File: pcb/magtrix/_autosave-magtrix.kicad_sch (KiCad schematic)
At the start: 24 parts, among them J2 Conn_01x03_Pin, J3 Conn_01x03_Pin, Q14 BUK6D120, Q15 BUK6D120-60PX

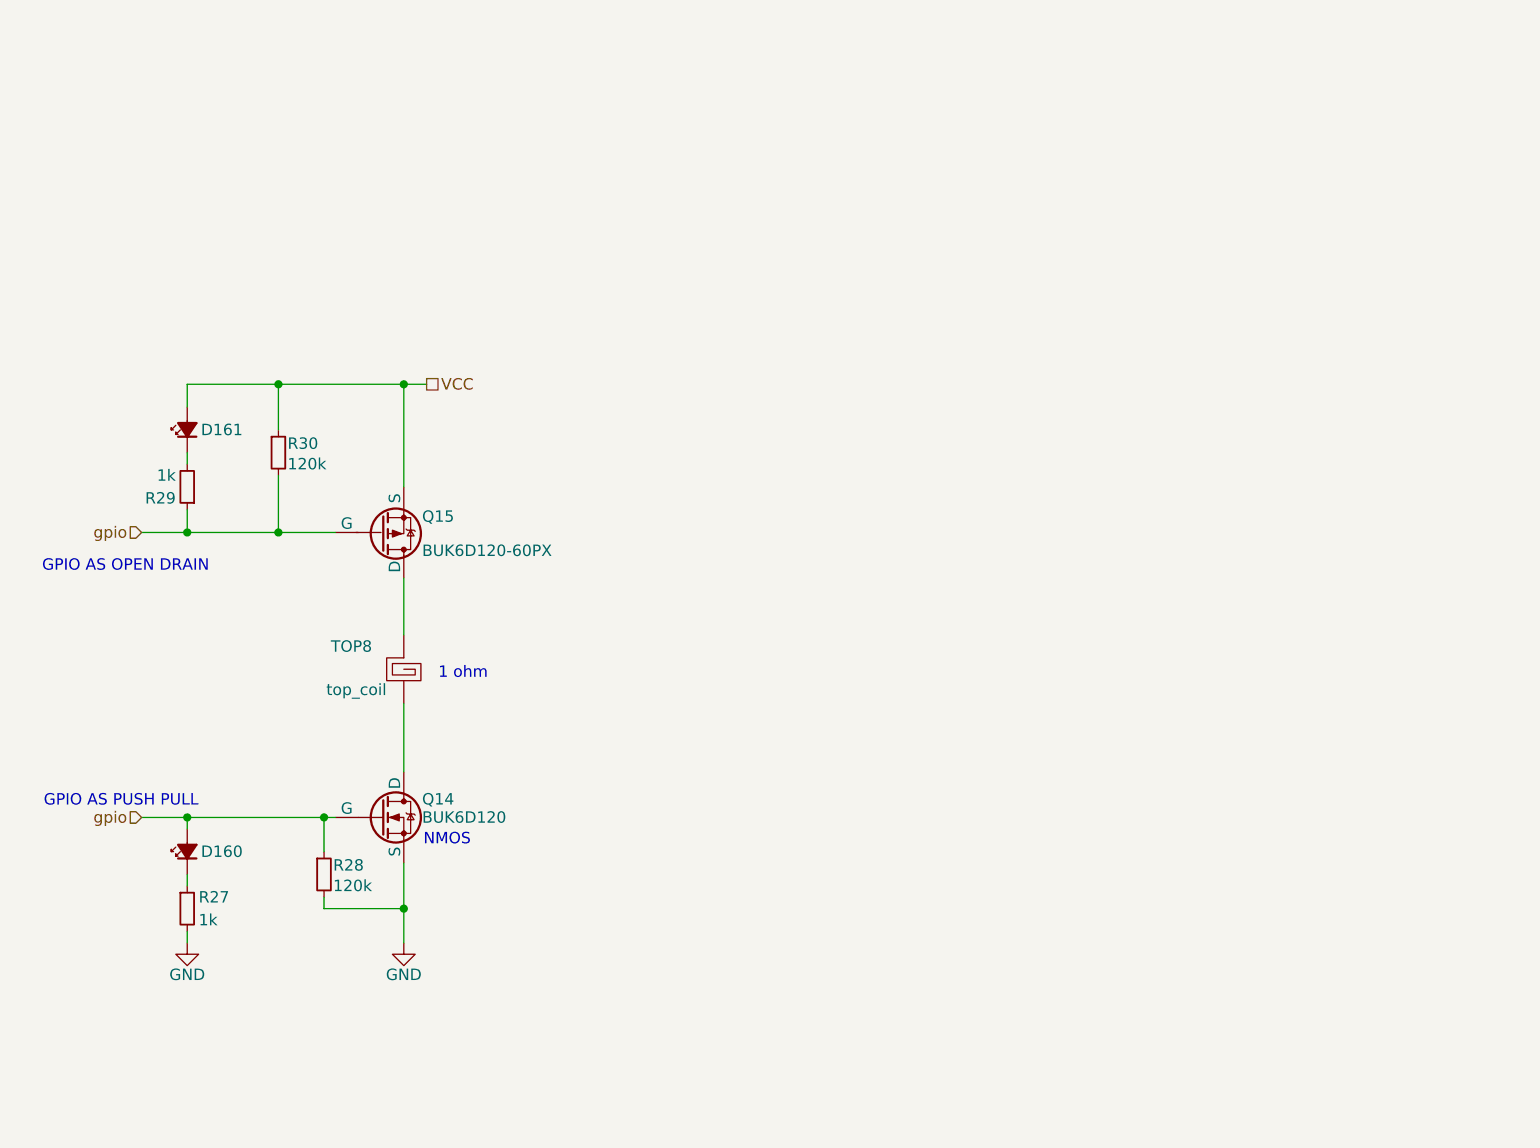
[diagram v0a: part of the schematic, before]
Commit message: Added debug pcb stuff
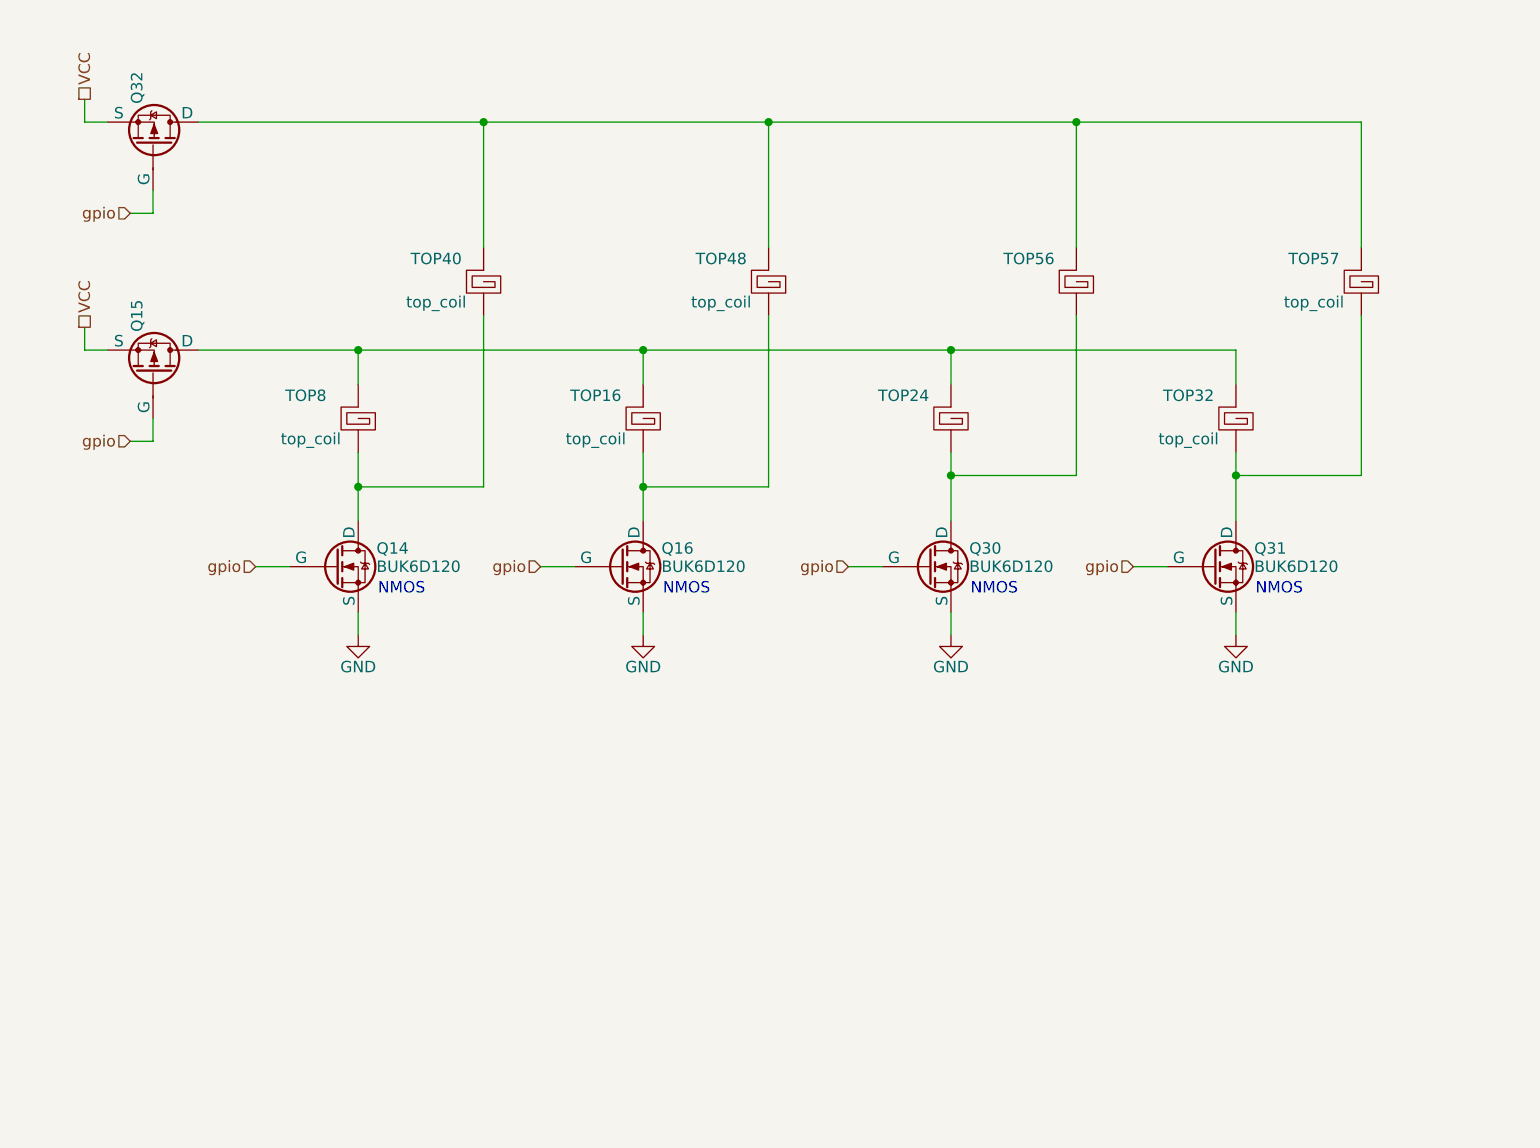
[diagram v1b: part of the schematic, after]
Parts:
- removed D160, D161: LED_Small_Filled, LED_SMD:LED_1206_3216Metric, symbol Device:LED_Small_Filled
- removed R27, R29: 1k, Resistor_SMD:R_1206_3216Metric, symbol Device:R_Small
- removed R28, R30: 120k, Resistor_SMD:R_1206_3216Metric, symbol Device:R_Small
- added Q16, Q30, Q31: BUK6D120, TRANSISTOR_NMOS:TRANS_BUK9D23-40EX, symbol Simulation_SPICE:NMOS
- added Q32: BUK6D120-60PX, TRANSISTOR_PMOS:BUK6D12060PX, symbol Simulation_SPICE:PMOS
- added TOP16, TOP24, TOP32, TOP40, TOP48, TOP56, TOP57: top_coil, libs:top_coil, symbol square_coils:top_coil
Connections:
- net GND: now also Q16.4 (S), Q16.8 (S), Q30.4 (S), Q30.8 (S), Q31.4 (S), Q31.8 (S)
- net VCC: now also Q32.4 (S), Q32.8 (S)
- net gpio: now also Q16.3 (G), Q30.3 (G), Q31.3 (G), Q32.3 (G)
- net at Q15.1 (D), Q15.2 (D), Q15.5 (D)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: now also TOP16.1 (A), TOP24.1 (A), TOP32.1 (A)
- net at Q14.1 (D), Q14.2 (D), Q14.5 (D)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: now also TOP40.2 (B)
- new net: Q32.1 (D), Q32.2 (D), Q32.5 (D), Q32.6 (D), Q32.7 (D), TOP40.1 (A), TOP48.1 (A), TOP56.1 (A), TOP57.1 (A)
- new net: Q30.1 (D), Q30.2 (D), Q30.5 (D), Q30.6 (D), Q30.7 (D), TOP24.2 (B), TOP56.2 (B)
- new net: Q16.1 (D), Q16.2 (D), Q16.5 (D), Q16.6 (D), Q16.7 (D), TOP16.2 (B), TOP48.2 (B)
- new net: Q31.1 (D), Q31.2 (D), Q31.5 (D), Q31.6 (D), Q31.7 (D), TOP32.2 (B), TOP57.2 (B)
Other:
- note removed: "1 ohm"
- note removed: "GPIO AS OPEN DRAIN"
- note removed: "GPIO AS PUSH PULL"
- moved on the sheet: Q14, Q15, TOP8
